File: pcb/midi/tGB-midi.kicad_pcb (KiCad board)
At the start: 2 copper layers, 25.2 x 31 mm, 25 parts, among them J1 MIDI_IN, J2 MIDI_THRU, J3 MIDI_OUT, J4 IO, U1 TLP2368, U2 TC7WZ07FK

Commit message: change C4 value from 10uF to 4.7uF
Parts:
- C4: value 10μ -> 4.7μ
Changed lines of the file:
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@@
       (effects (font (size 0.6 0.6) (thickness 0.12)))
     )
-    (fp_text value "10μ" (at 0 1.16 90) (layer "F.Fab")
+    (fp_text value "4.7μ" (at 0 1.16 90) (layer "F.Fab")
       (effects (font (size 0.6 0.6) (thickness 0.12)))
     )

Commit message: add comment, fix power net name
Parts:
- C2, C3: value 0.1μ -> 0.1μF
- C4: value 4.7μ -> 4.7μF
- J4: value IO -> PROG_PORT
- R7: value 100k -> 100kΩ
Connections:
- net +3.3V renamed +3V3
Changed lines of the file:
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@@
   (net 15 "Net-(FB6-Pad1)")
   (net 16 "Net-(FB6-Pad2)")
-  (net 17 "+3.3V")
+  (net 17 "+3V3")
   (net 18 "/MIDI_RX")
   (net 19 "/MIDI_TX")
@@
     (fp_line (start 0.525 0.27) (end -0.525 0.27) (layer "F.Fab") (width 0.1))
     (pad "1" smd roundrect (at -0.51 0 90) (size 0.54 0.64) (layers "F.Cu" "F.Paste" "F.Mask") (roundrect_rratio 0.25)
-      (net 17 "+3.3V") (pintype "passive"))
+      (net 17 "+3V3") (pintype "passive"))
     (pad "2" smd roundrect (at 0.51 0 90) (size 0.54 0.64) (layers "F.Cu" "F.Paste" "F.Mask") (roundrect_rratio 0.25)
       (net 18 "/MIDI_RX") (pintype "passive"))
@@
       (effects (font (size 0.6 0.6) (thickness 0.12)))
     )
-    (fp_text value "IO" (at 0 -2.54) (layer "F.Fab")
+    (fp_text value "PROG_PORT" (at 0 -2.54) (layer "F.Fab")
       (effects (font (size 0.6 0.6) (thickness 0.12)))
     )
@@
       (net 3 "+5V") (pinfunction "Pin_1") (pintype "passive"))
     (pad "2" smd rect (at 2.54 0) (size 1.7 3.25) (layers "F.Cu" "F.Mask")
-      (net 17 "+3.3V") (pinfunction "Pin_2") (pintype "passive"))
+      (net 17 "+3V3") (pinfunction "Pin_2") (pintype "passive"))
     (pad "2" thru_hole rect (at 2.54 0.775) (size 1.7 1.7) (drill 1) (layers *.Cu *.Mask)
-      (net 17 "+3.3V") (pinfunction "Pin_2") (pintype "passive"))
+      (net 17 "+3V3") (pinfunction "Pin_2") (pintype "passive"))
     (pad "3" smd rect (at 5.08 0) (size 1.7 3.25) (layers "F.Cu" "F.Mask")
       (net 1 "GND") (pinfunction "Pin_3") (pintype "passive"))
@@
       (effects (font (size 0.6 0.6) (thickness 0.12)))
     )
-    (fp_text value "0.1μ" (at 0 1.16) (layer "F.Fab")
+    (fp_text value "0.1μF" (at 0 1.16) (layer "F.Fab")
       (effects (font (size 0.6 0.6) (thickness 0.12)))
     )
@@
       (effects (font (size 0.6 0.6) (thickness 0.12)))
     )
-    (fp_text value "100k" (at 0 1.17) (layer "F.Fab")
+    (fp_text value "100kΩ" (at 0 1.17) (layer "F.Fab")
       (effects (font (size 0.6 0.6) (thickness 0.12)))
     )
@@
     (fp_line (start 0.525 -0.27) (end 0.525 0.27) (layer "F.Fab") (width 0.1))
     (pad "1" smd roundrect (at -0.51 0) (size 0.54 0.64) (layers "F.Cu" "F.Paste" "F.Mask") (roundrect_rratio 0.25)
-      (net 17 "+3.3V") (pintype "passive"))
+      (net 17 "+3V3") (pintype "passive"))
     (pad "2" smd roundrect (at 0.51 0) (size 0.54 0.64) (layers "F.Cu" "F.Paste" "F.Mask") (roundrect_rratio 0.25)
       (net 19 "/MIDI_TX") (pintype "passive"))
@@
       (effects (font (size 0.6 0.6) (thickness 0.12)))
     )
-    (fp_text value "0.1μ" (at 0 1.16 -270) (layer "F.Fab")
+    (fp_text value "0.1μF" (at 0 1.16 -270) (layer "F.Fab")
       (effects (font (size 0.6 0.6) (thickness 0.12)))
     )
@@
       (effects (font (size 0.6 0.6) (thickness 0.12)))
     )
-    (fp_text value "4.7μ" (at 0 1.16 90) (layer "F.Fab")
-      (effects (font (size 0.6 0.6) (thickness 0.12)))
-    )
+    (fp_text value "4.7μF" (at 0 1.16 90) (layer "F.Fab")
+      (effects (font (size 0.6 0.6) (thickness 0.12)))
+    )

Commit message: set title and revision
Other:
- board text added: "PCB thickness: 0.8mm"
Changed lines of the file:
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@@
   )
   (paper "A4")
+  (title_block
+    (title "tsuraraGB MIDI Adapter PCB")
+    (rev "A")
+  )
   (layers
     (0 "F.Cu" signal)
@@
     (effects (font (size 0.6 0.6) (thickness 0.12)))
   )
+  (gr_text "PCB thickness: 0.8mm" (at 87.7 102.5) (layer "Dwgs.User")
+    (effects (font (size 0.6 0.6) (thickness 0.12)) (justify left))
+  )
   (dimension (type aligned) (layer "Dwgs.User")

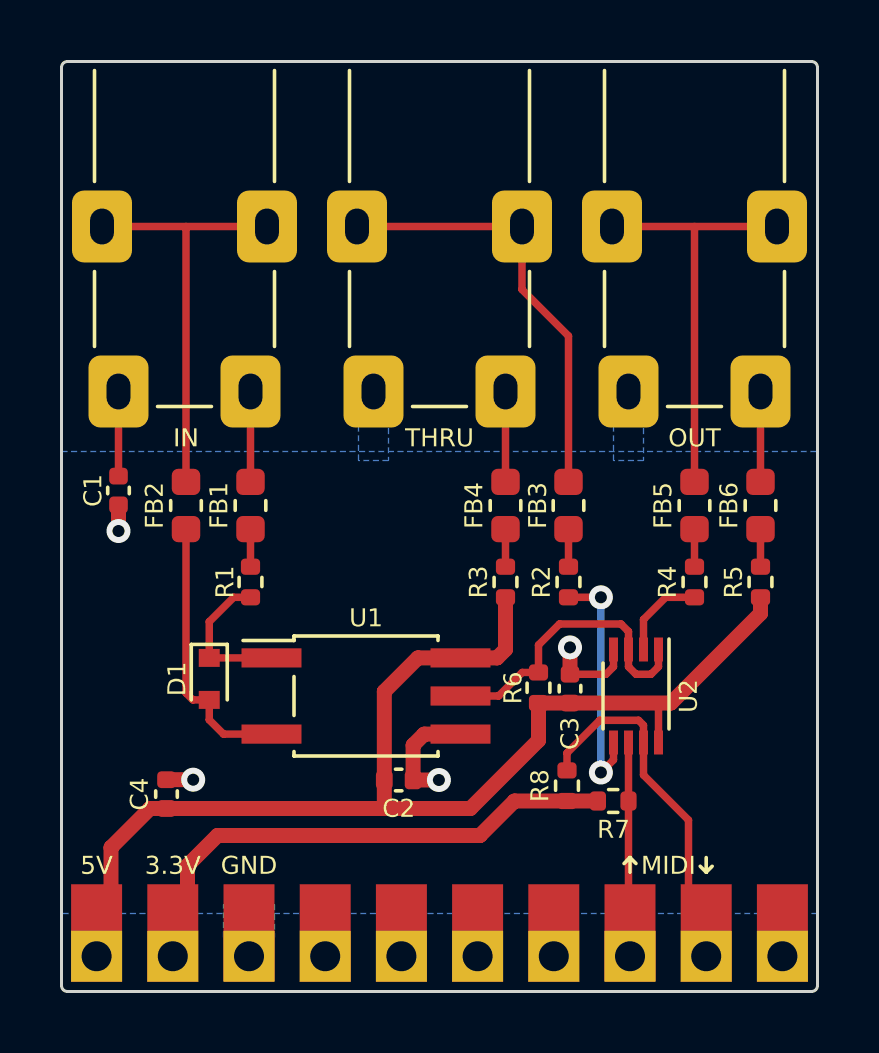
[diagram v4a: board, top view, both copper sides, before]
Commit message: migrate KiCad 7 -> 10
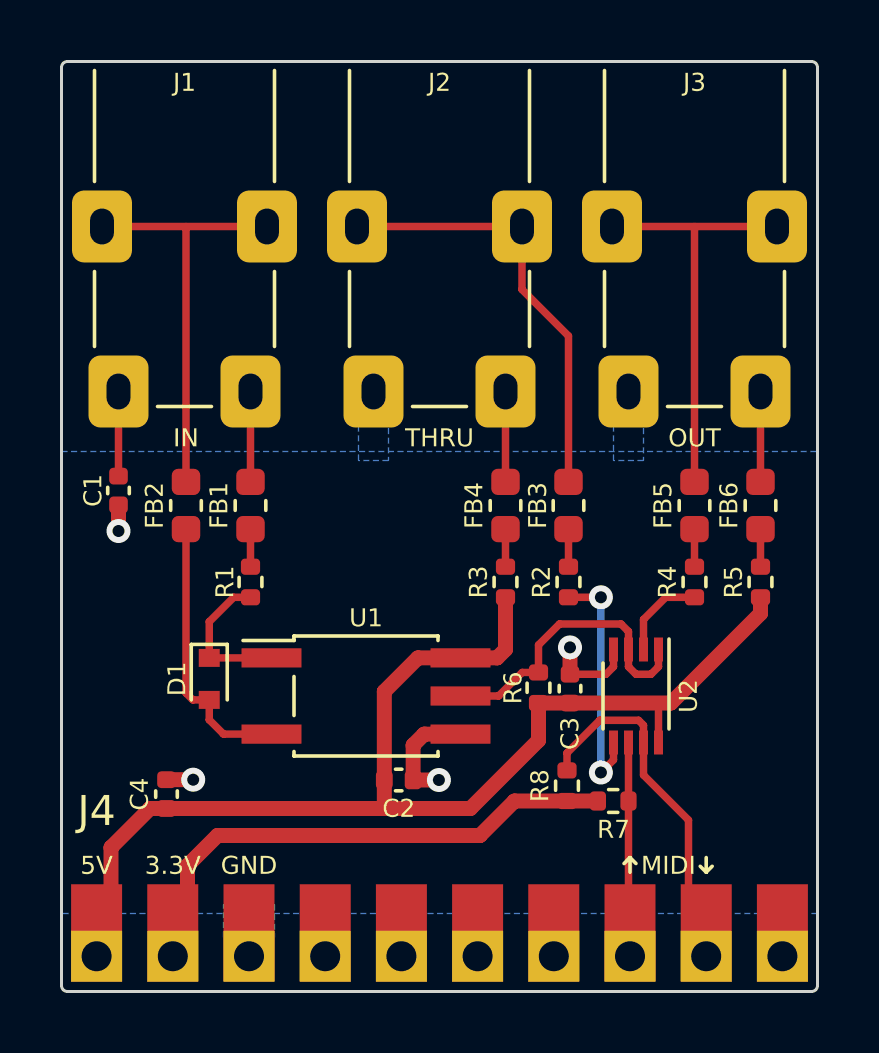
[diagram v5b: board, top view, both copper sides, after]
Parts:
- J1, J2, J3: footprint MJ-8435:MJ-8435 -> ProjectSpecific:MJ-8435
- J4: footprint Pin_Sidemount:PinSocket_1x10_P2.54_Sidemount -> ProjectSpecific:PinSocket_1x10_P2.54_Sidemount
- U1: footprint Package_SO:SO-5_4.4x3.6mm_P1.27mm -> ProjectSpecific:SO-5_4.4x3.6mm_P1.27mm
- U2: footprint Package_SO:VSSOP-8_2.3x2mm_P0.5mm -> ProjectSpecific:VSSOP-8_2.3x2mm_P0.5mm
